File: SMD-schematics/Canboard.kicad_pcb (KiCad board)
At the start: 2 copper layers, 0 parts

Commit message: "placing the footprints in PCB design no trakes yet"
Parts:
- added C1: .33uf, Capacitors_SMD:CP_Elec_8x6.5, F.Cu at (134.7, 78.7)
- added C10: 1uf, Capacitors_SMD:CP_Elec_8x6.5, F.Cu at (125.7, 111.8)
- added C11: 1uf, Capacitors_SMD:CP_Elec_8x6.5, F.Cu at (138.4, 111.8)
- added C12: 1uf, Capacitors_SMD:CP_Elec_8x6.5, F.Cu at (111.1, 111.1)
- added C13: 1uf, Capacitors_SMD:CP_Elec_8x6.5, F.Cu at (133.9, 123.8)
- added C14: 1uf, Capacitors_SMD:CP_Elec_8x6.5, F.Cu at (121.4, 123.8)
- added C2: .1uf, Capacitors_SMD:CP_Elec_8x6.7, F.Cu at (167.1, 79.4)
- added C6: .1uf, Capacitors_SMD:CP_Elec_8x6.5, F.Cu at (91.3, 67.3)
- added C7: .1uf, Capacitors_SMD:CP_Elec_8x6.5, F.Cu at (123.8, 94.0)
- added C8: 22pf, Capacitors_SMD:C_0805_HandSoldering, F.Cu at (151.8, 138.4)
- added C9: 22pf, Capacitors_SMD:C_0805_HandSoldering, F.Cu at (157.5, 138.4)
- added D1: LED, LEDs:LED_0805_HandSoldering, F.Cu at (145.3, 79.4)
- added D2: LED, LEDs:LED_0805_HandSoldering, F.Cu at (160.0, 104.1)
- added D3: LED, LEDs:LED_0805_HandSoldering, F.Cu at (169.5, 126.4)
- added D4: LED, LEDs:LED_0805_HandSoldering, F.Cu at (169.6, 129.5)
- added D5: LED, LEDs:LED_0805_HandSoldering, F.Cu at (169.5, 122.6)
- added J1: Barrel_Jack, Connectors:JACK_ALIM, F.Cu at (151.1, 73.0)
- added J11: Conn_02x06_Odd_Even, Pin_Headers:Pin_Header_Straight_2x06_Pitch2.54mm, F.Cu at (131.4, 136.5)
- added J12: Conn_02x06_Odd_Even, Pin_Headers:Pin_Header_Straight_2x06_Pitch2.54mm, F.Cu at (167.6, 139.1)
- added J2: Screw_Terminal_01x02, TerminalBlocks_Phoenix:TerminalBlock_Phoenix_MKDS1.5-2pol, F.Cu at (132.8, 65.4)
- added J3: USB_OTG, Connectors_USB:USB_Micro-B_Molex-105017-0001, F.Cu at (162.2, 65.1)
- added J4: Conn_Debug, Pin_Headers:Pin_Header_Straight_2x03_Pitch2.54mm, F.Cu at (177.8, 82.5)
- added J5: Screw_Terminal_01x02, TerminalBlocks_Phoenix:TerminalBlock_Phoenix_MKDS1.5-2pol, F.Cu at (106.0, 65.4)
- added J6: DB9_Female, Connectors_DSub:DB9FC, F.Cu at (99.7, 100.1)
- added J7: Conn_02x06_Odd_Even, Pin_Headers:Pin_Header_Straight_2x06_Pitch2.54mm, F.Cu at (178.4, 97.2)
- added J8: Conn_02x06_Odd_Even, Pin_Headers:Pin_Header_Straight_2x06_Pitch2.54mm, F.Cu at (178.4, 116.2)
- added J9: DB9_Female, Connectors_DSub:DB9FC, F.Cu at (103.0, 120.0)
- added JP1: Jumper_NO_Small, Pin_Headers:Pin_Header_Straight_1x02_Pitch2.54mm, F.Cu at (177.8, 92.7)
- added JP2: Jumper_NO_Small, Pin_Headers:Pin_Header_Straight_1x02_Pitch2.54mm, F.Cu at (180.3, 78.1)
- added JP3: Jumper_NO_Small, Pin_Headers:Pin_Header_Straight_1x02_Pitch2.54mm, F.Cu at (123.8, 84.5)
- added JP4: Jumper_NO_Small, Pin_Headers:Pin_Header_Straight_1x02_Pitch2.54mm, F.Cu at (110.5, 74.3)
- added JP5: Jumper_NO_Small, Pin_Headers:Pin_Header_Straight_1x02_Pitch2.54mm, F.Cu at (134.6, 92.7)
- added R1: 100k, Resistors_SMD:R_1206_HandSoldering, F.Cu at (154.2, 79.4)
- added R10: 320, Resistors_SMD:R_1206_HandSoldering, F.Cu at (145.5, 83.8)
- added R11: 320, Resistors_SMD:R_1206_HandSoldering, F.Cu at (135.3, 87.6)
- added R12: 1K, Resistors_SMD:R_1206_HandSoldering, F.Cu at (151.9, 109.2)
- added R13: 320, Resistors_SMD:R_1206_HandSoldering, F.Cu at (151.7, 104.1)
- added R14: 320, Resistors_SMD:R_1206_HandSoldering, F.Cu at (163.8, 132.2)
- added R15: 1K, Resistors_SMD:R_1206_HandSoldering, F.Cu at (160.1, 109.2)
- added R16: 320, Resistors_SMD:R_1206_HandSoldering, F.Cu at (163.8, 121.2)
- added R2: 1k, Resistors_SMD:R_1206_HandSoldering, F.Cu at (154.2, 83.8)
- added R5: 1K, Resistors_SMD:R_1206_HandSoldering, F.Cu at (111.2, 100.3)
- added R8: 120, Resistors_SMD:R_1206_HandSoldering, F.Cu at (109.3, 81.3)
- added R9: 12k, Resistors_SMD:R_1206_HandSoldering, F.Cu at (136.4, 97.2)
- added SW1: SW_Push_Dual, Buttons_Switches_THT:Push_E-Switch_KS01Q01, F.Cu at (146.1, 90.8)
- added SW2: SW_Push_Dual, Buttons_Switches_THT:Push_E-Switch_KS01Q01, F.Cu at (172.7, 63.6)
- added SW3: SW_Push_Dual, Buttons_Switches_THT:Push_E-Switch_KS01Q01, F.Cu at (161.3, 90.2)
- added U1: L7805, TO_SOT_Packages_THT:TO-220-3_Horizontal, F.Cu at (119.4, 79.5)
- added U2: ATMEGA32M1-AU, Housings_QFP:TQFP-32_7x7mm_Pitch0.8mm, F.Cu at (154.5, 119.8)
- added U3: MCP2551-I/P, Housings_SOIC:SOIC-8_3.9x4.9mm_Pitch1.27mm, F.Cu at (111.1, 92.1)
- added U5: MAX232, Housings_SOIC:SOIC-16_3.9x9.9mm_Pitch1.27mm, F.Cu at (121.9, 135.9)
- added Y2: 16Mhz, Crystals:Crystal_HC49-U_Vertical, F.Cu at (152.0, 132.1)

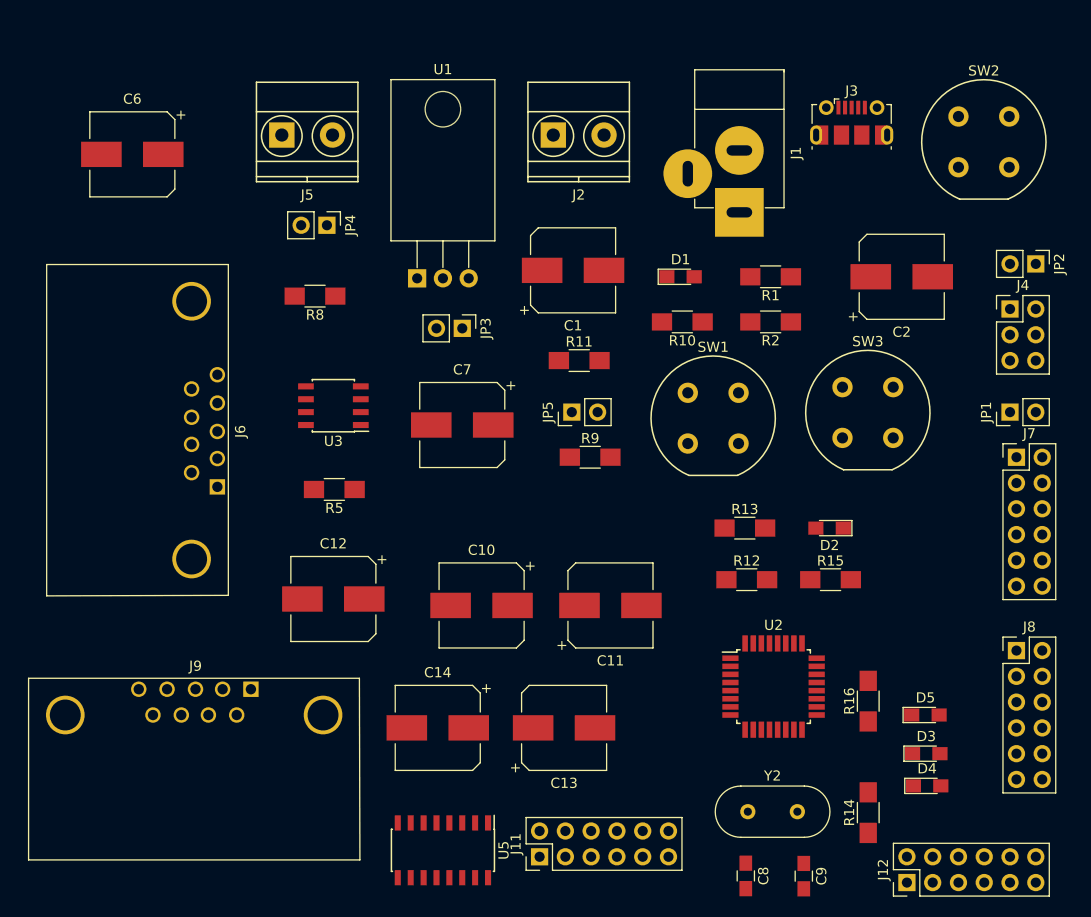
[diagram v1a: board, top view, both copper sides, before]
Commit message: "size of PCB 8*8 before tracking"
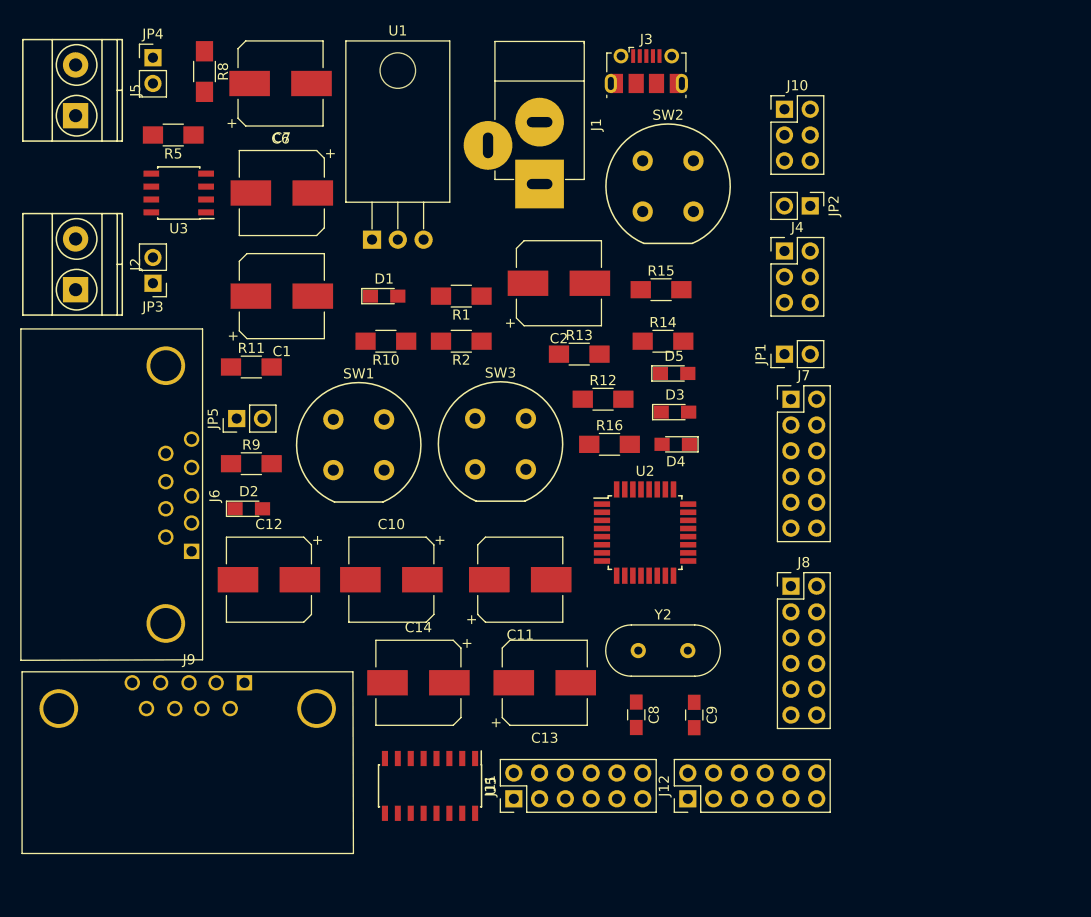
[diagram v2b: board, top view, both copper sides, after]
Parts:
- added J10: Conn_02x03_Odd_Even, Pin_Headers:Pin_Header_Straight_2x03_Pitch2.54mm, F.Cu at (155.6, 62.9)
- moved D2 57.3 mm to (102.8, 102.2), turned to 0 degrees
- moved R14 50.7 mm to (143.6, 85.7), turned to 0 degrees
- moved J2 49.5 mm to (85.7, 80.6), turned to 90 degrees
- moved D5 41.8 mm to (144.7, 88.9)
- moved D3 41.8 mm to (144.8, 92.7)
- moved D4 41.8 mm to (144.9, 95.9), turned to 180 degrees
- moved R5 38.4 mm to (95.3, 65.4)
- moved SW3 36.3 mm to (125.1, 93.3)
- moved R16 35.9 mm to (138.3, 95.9), turned to 0 degrees
- moved SW1 35.0 mm to (111.1, 93.4)
- moved C2 33.8 mm to (133.3, 80.0)
- moved R9 33.4 mm to (103.0, 97.8)
- moved R15 33.1 mm to (143.4, 80.6)
- moved JP5 33.0 mm to (101.6, 93.3)
- moved R11 32.3 mm to (103.0, 88.3)
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
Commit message: adding lin circuit to the scgematic without the diode
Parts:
- removed C1: .33uf, Capacitors_SMD:CP_Elec_8x6.5
- removed C10, C11, C12, C13, C14: 1uf, Capacitors_SMD:CP_Elec_8x6.5
- removed C2: .1uf, Capacitors_SMD:CP_Elec_8x6.7
- removed C6, C7: .1uf, Capacitors_SMD:CP_Elec_8x6.5
- removed C8, C9: 22pf, Capacitors_SMD:C_0805_HandSoldering
- removed D1, D2, D3, D4, D5: LED, LEDs:LED_0805_HandSoldering
- removed J1: Barrel_Jack, Connectors:JACK_ALIM
- removed J10: Conn_02x03_Odd_Even, Pin_Headers:Pin_Header_Straight_2x03_Pitch2.54mm
- removed J11, J12, J7, J8: Conn_02x06_Odd_Even, Pin_Headers:Pin_Header_Straight_2x06_Pitch2.54mm
- removed J2, J5: Screw_Terminal_01x02, TerminalBlocks_Phoenix:TerminalBlock_Phoenix_MKDS1.5-2pol
- removed J3: USB_OTG, Connectors_USB:USB_Micro-B_Molex-105017-0001
- removed J4: Conn_Debug, Pin_Headers:Pin_Header_Straight_2x03_Pitch2.54mm
- removed J6, J9: DB9_Female, Connectors_DSub:DB9FC
- removed JP1, JP2, JP3, JP4, JP5: Jumper_NO_Small, Pin_Headers:Pin_Header_Straight_1x02_Pitch2.54mm
- removed R1: 100k, Resistors_SMD:R_1206_HandSoldering
- removed R10, R11, R13, R14, R16: 320, Resistors_SMD:R_1206_HandSoldering
- removed R12, R15, R5: 1K, Resistors_SMD:R_1206_HandSoldering
- removed R2: 1k, Resistors_SMD:R_1206_HandSoldering
- removed R8: 120, Resistors_SMD:R_1206_HandSoldering
- removed R9: 12k, Resistors_SMD:R_1206_HandSoldering
- removed SW1, SW2, SW3: SW_Push_Dual, Buttons_Switches_THT:Push_E-Switch_KS01Q01
- removed U1: L7805, TO_SOT_Packages_THT:TO-220-3_Horizontal
- removed U2: ATMEGA32M1-AU, Housings_QFP:TQFP-32_7x7mm_Pitch0.8mm
- removed U3: MCP2551-I/P, Housings_SOIC:SOIC-8_3.9x4.9mm_Pitch1.27mm
- removed U5: MAX232, Housings_SOIC:SOIC-16_3.9x9.9mm_Pitch1.27mm
- removed Y2: 16Mhz, Crystals:Crystal_HC49-U_Vertical
